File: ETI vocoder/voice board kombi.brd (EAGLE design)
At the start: 160 x 100 mm, 94 parts, among them IC1 TL072P, IC2 TL072P, IC3 TL081P, IC4 TL081P, IC5 TL072P, IC6 LM13600AN, IC7 TL072P, Q1 BF244, Q2 BC214

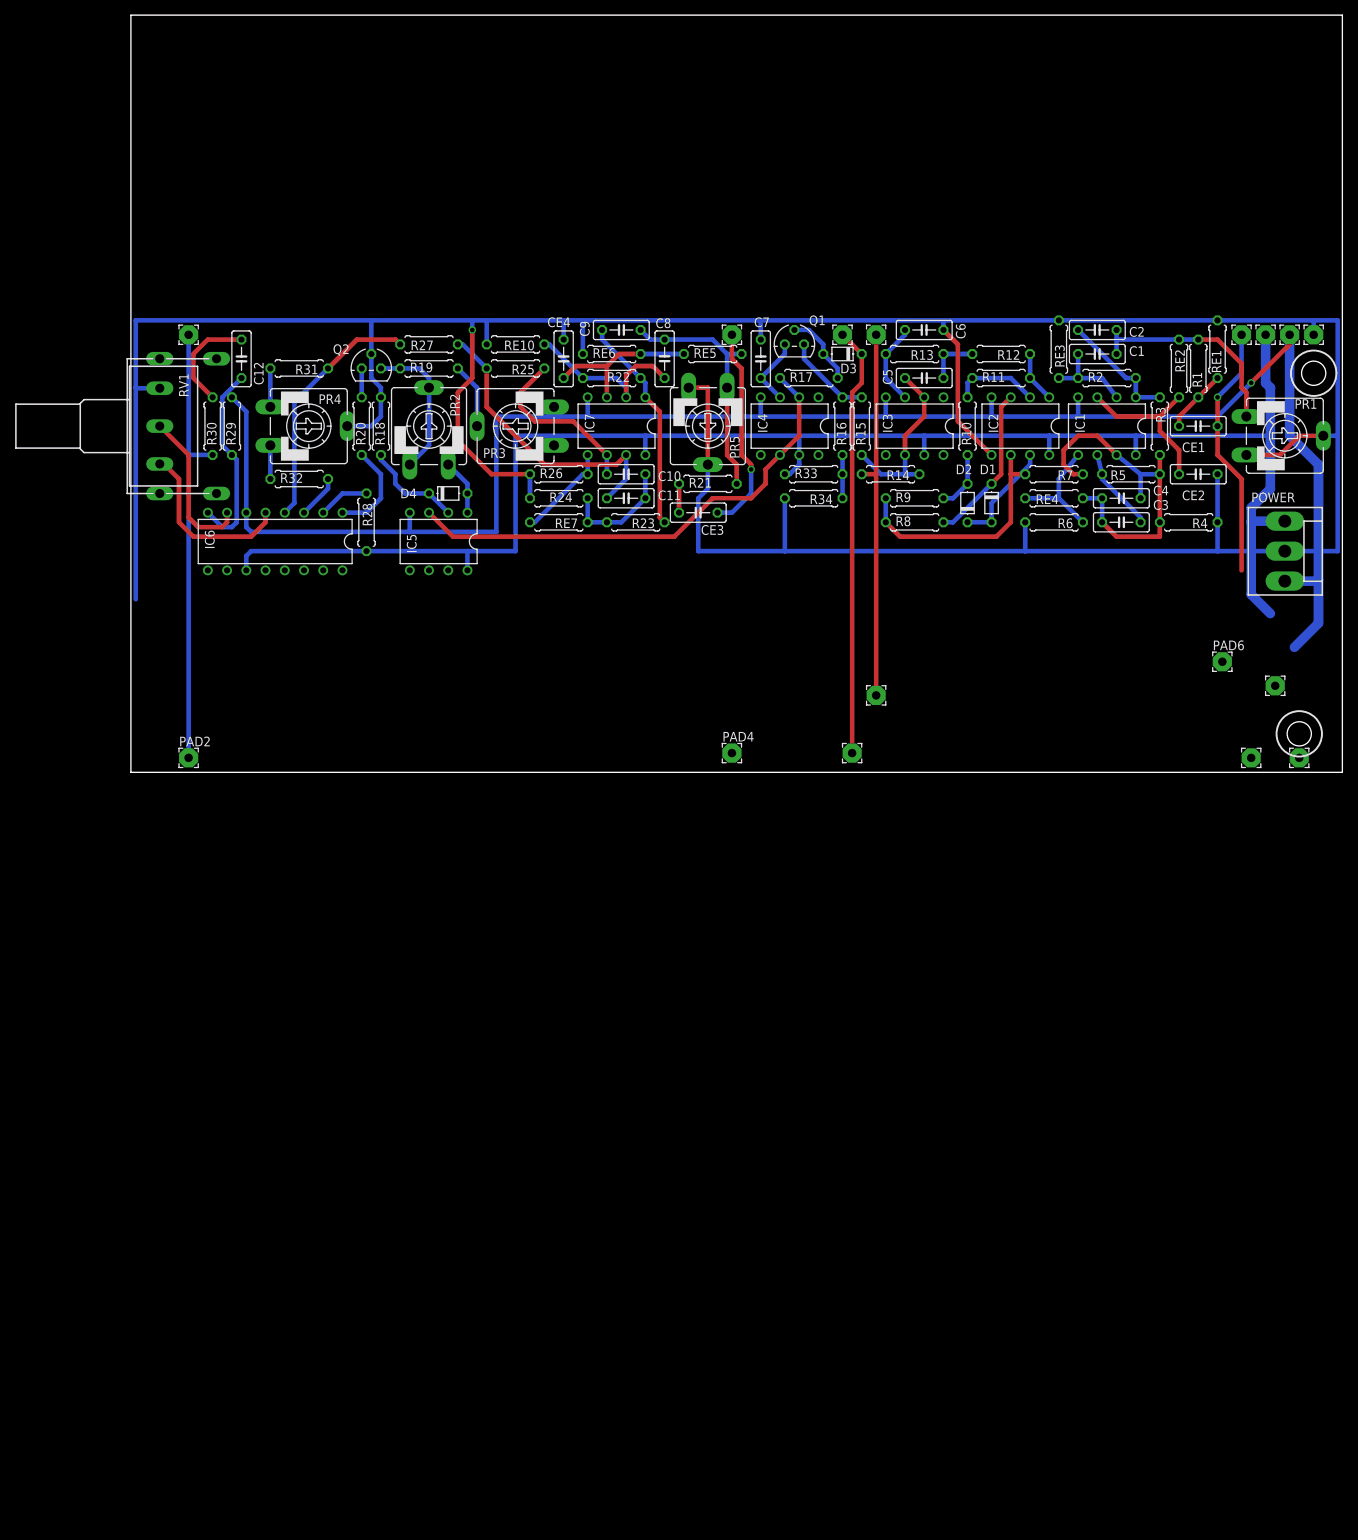
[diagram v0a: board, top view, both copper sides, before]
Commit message: Duplicated all parts, ready for creating channel 2 (after main computer bailed on me and I lost a days work)
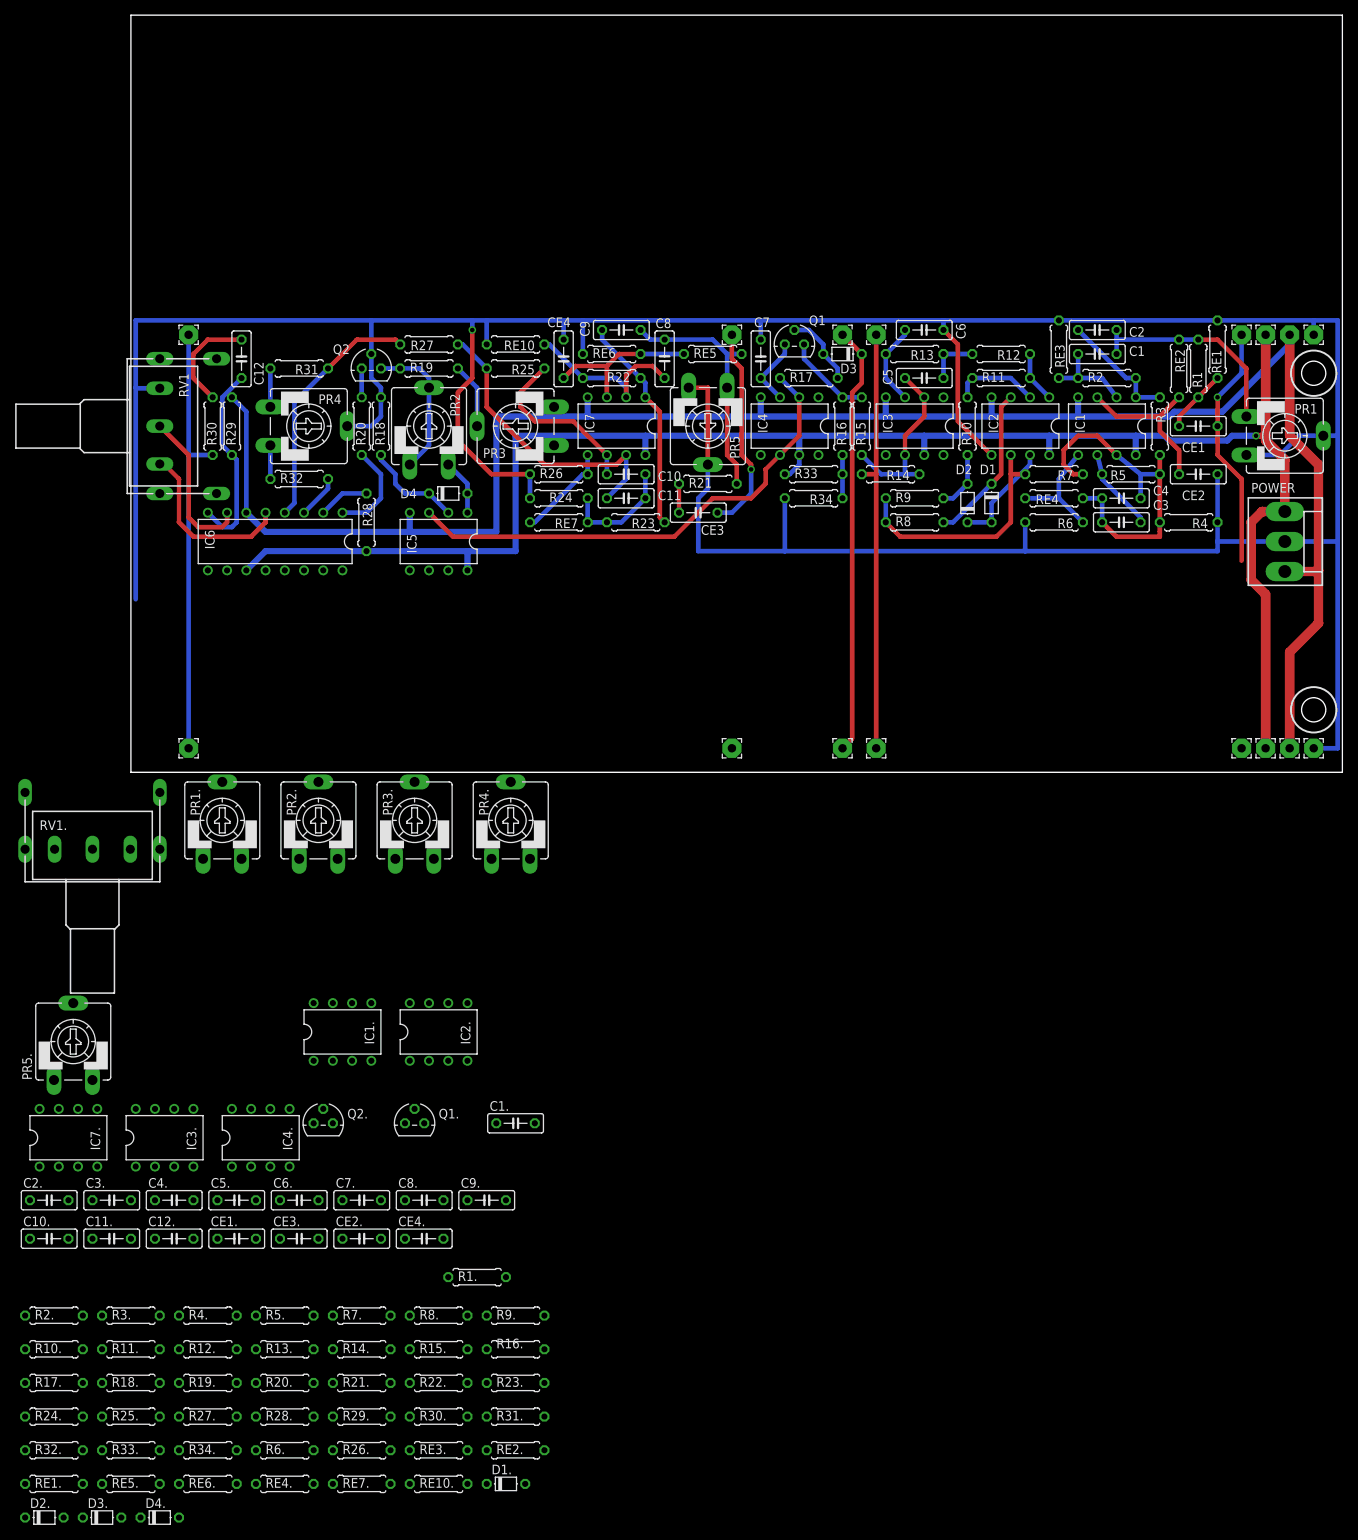
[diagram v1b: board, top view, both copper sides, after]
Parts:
- added C1., C10., C11., C12., C2., C3., C4., C5., C6., C7., C8., C9., CE1., CE2., CE3., CE4.: (no value), resistor:C050-025X075
- added D1., D2., D3., D4.: (no value), diode:D-5
- added IC1., IC2., IC7.: TL072P, linear:DIL08
- added IC3., IC4.: TL081P, linear:DIL08
- added PR1., PR2., PR3., PR4., PR5.: (no value), pot:CA9V
- added Q1.: BF244, transistor-fet:TO-92
- added Q2.: BC214, transistor-pnp:TO92
- added R1., R10., R11., R12., R13., R14., R15., R16., R17., R18., R19., R2., R20., R21., R22., R23., R24., R25., R26., R27., R28., R29., R3., R30., R31., R32., R33., R34., R4., R5., R6., R7., R8., R9., RE1., RE10., RE2., RE3., RE4., RE5., RE6., RE7.: (no value), resistor:0207/7
- added RV1.: 100k log, joakim:POT16_W_BRACKET
- moved PAD6 11.7 mm to (146.7, 3.17)
- moved PAD14 8.47 mm to (153.0, 3.17)
- moved PAD8 6.99 mm to (98.4, 3.17)
- moved PAD16 2.29 mm to (156.2, 3.17)
- moved PAD9 2.29 mm to (149.9, 3.17)
- moved PAD11 1.42 mm to (94.0, 3.17)
- moved PAD2 1.27 mm to (7.62, 3.17)
- moved POWER 1.27 mm to (152.4, 30.5)
- moved PAD4 0.63 mm to (79.4, 3.17)
- flipped PAD13 to the bottom
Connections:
- new net BIAS2: R16..1, R33..1, R34..2
- new net N$47: C1..2, IC1..2, R2..1, RE3..2
- new net N$48: C1..1, C2..1, PR1..A, R1..2, RE2..1
- new net N$49: C2..2, IC1..1, R2..2, R3..1
- new net N$50: C3..1, C4..1, R3..2, R4..2, RE4..1
- new net N$51: C3..2, IC1..6, R5..2
- new net N$52: IC1..5, R6..2, RE4..2
- new net N$53: C4..2, IC1..7, R5..1, R7..1
- new net N$54: IC2..6, R7..2, R8..1, R9..1
- new net N$55: D1..C, IC2..3, R8..2
- new net N$56: D1..A, D2..C, IC2..7
- new net N$57: D2..A, R10..1, R9..2
- new net N$58: IC2..2, R10..2, R11..1
- new net N$59: IC2..1, R11..2, R12..1
- new net N$60: C5..2, R12..2, R13..1
- new net N$61: C5..1, IC3..2, IC3..6, R14..1, R15..2
- new net N$62: C6..2, IC3..3, R13..2
- new net N$63: Q1..3, R15..1, R16..2
- new net N$64: C7..2, IC4..3, Q1..1
- new net N$65: D3..A, Q1..2, R17..2
- new net N$66: IC4..2, IC4..6, IC5.5, R17..1
- new net N$67: D4..C, IC5.6, R18..1
- new net N$68: D4..A, IC5.7, PR2..E
- new net N$69: PR2..A, PR2..S, Q2..1, R19..1
- new net N$70: PR3..S, R19..2
- new net N$71: Q2..3, R20..2
- new net N$72: PR4..A, R31..2
- new net N$73: C8..2, C9..2, PR5..A, R21..2, RE5..1
- new net N$74: C10..2, C11..2, R23..2, R24..2, RE7..1
- new net N$75: C8..1, IC7..2, R22..1, RE10..2
- new net N$76: C9..1, IC7..1, R22..2, R23..1
- new net N$77: C11..1, IC7..7, R25..2, R27..1
- new net N$78: PR4..E, R32..1
- new net N$79: IC6.14, R32..2
- new net N$80: IC6.15, R28..1
- new net N$81: IC6.13, R27..2, R31..1
- new net N$82: IC6.16, R20..1
- new net N$83: IC6.10, RV1..1S
- new net N$84: C12..2, IC6.9, R29..1
- new net N$85: C12..1, R30..1
- new net N$86: C10..1, IC7..6, R25..1
- new net N$87: IC7..5, R26..2, RE7..2
- new net N$88: CE1..2, R1..1, RE1..2
- new net N$89: CE2..2, IC1..3, RE2..2
- new net N$90: CE3..2, R21..1
- new net N$91: CE4..2, IC7..3, RE5..2, RE6..2
- new net N$92: IC6.12, RV1..1E
- net +12V: now also IC1..8, IC2..8, IC3..7, IC4..7, IC7..8, PR3..A, R28..2, R33..2
- net -12V: now also IC1..4, IC2..4, IC3..4, IC4..4, IC7..4, PR3..E, R29..2
- net EXITATION_IN: now also CE3..1
- net GND: now also C6..1, C7..1, CE2..1, CE4..1, IC2..5, PR1..E, PR1..S, PR4..S, PR5..E, PR5..S, Q2..2, R18..2, R24..1, R26..1, R34..1, R4..1, R6..1, RE1..1, RE10..1, RE3..1, RE6..1, RV1..1A
- net OUTPUT_AMP: now also R30..2
- net SLEW_RATE_CTRL: now also D3..C
- net SPEECH_IN: now also CE1..1
- net VU_DETECTOR: now also R14..2
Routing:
- net GND: track 457.5 -> 486.7 mm
- net +12V: track 216.6 -> 231.7 mm, vias 0 -> 1
- net -12V: track 241.9 -> 254.1 mm, vias 1 -> 0
- net VU_DETECTOR: track 49.5 -> 56.5 mm
- net SPEECH_IN: track 33.7 -> 32.5 mm
- net OUTPUT_AMP: track 59.1 -> 57.8 mm

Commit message: Finished laying out most duplicated components
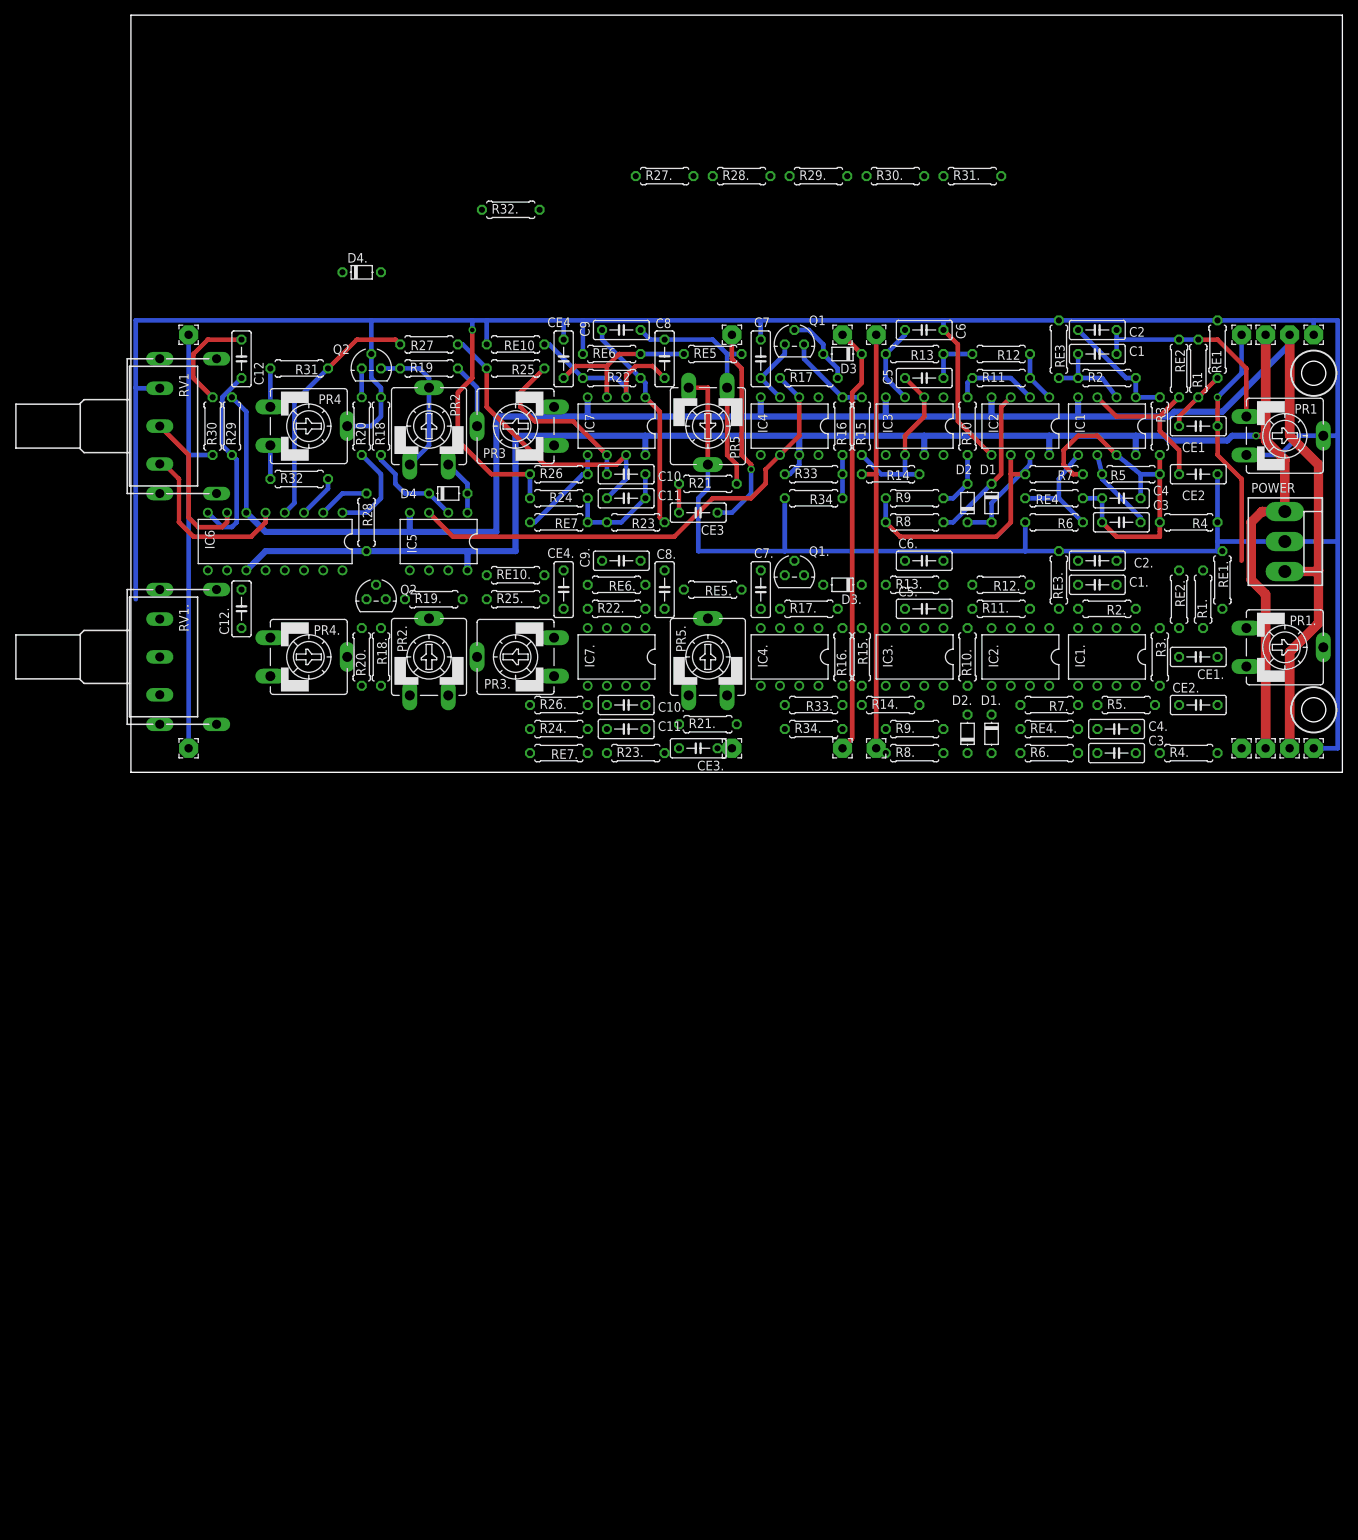
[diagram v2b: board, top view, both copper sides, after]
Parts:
- moved RE1. 195.1 mm to (144.1, 25.4), turned to 270 degrees
- moved R27. 174.6 mm to (70.5, 78.7)
- moved R28. 174.6 mm to (80.6, 78.7)
- moved R29. 174.6 mm to (90.8, 78.7)
- moved R30. 174.6 mm to (101.0, 78.7)
- moved R31. 174.6 mm to (111.1, 78.7)
- moved R32. 174.6 mm to (50.2, 74.3)
- moved R2. 167.5 mm to (128.9, 21.6), turned to 180 degrees
- moved D4. 166.6 mm to (30.5, 66.0)
- moved C2. 162.2 mm to (127.6, 27.9), turned to 180 degrees
- moved R3. 161.4 mm to (135.9, 15.2), turned to 270 degrees
- moved D2. 159.9 mm to (110.5, 5.08), turned to 90 degrees
- moved D3. 157.3 mm to (94.0, 24.8), turned to 180 degrees
- moved R10. 151.4 mm to (110.5, 15.2), turned to 90 degrees
- moved R11. 150.9 mm to (114.9, 21.6)
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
